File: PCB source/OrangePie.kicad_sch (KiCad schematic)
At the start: 0 parts

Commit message: Do Cleanup
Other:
- sheet 5v buck ports: added BUCK_OUT, Pgood, V_{IN}; removed 5V_OUT, Vin

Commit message: Pass ERC
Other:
- sheet DIN41612 connector ports: added 5v_STDBY, GPIOR[0..13]; removed GPIOR[0..15], STDBY OUT
- sheet FAN controller ports: added 12V_IN; removed none
- sheet OrangePi 5 pro Header ports: added BUCK_EN; removed none
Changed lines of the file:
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@@
 		(comment 2 "DESIGNED IN POLAND")
+	)
+	(junction
+		(at 67.31 138.43)
+		(diameter 0)
+		(color 0 0 0 0)
+	)
+	(junction
+		(at 135.89 142.24)
+		(diameter 0)
+		(color 0 0 0 0)
 	)
 	(no_connect
@@
 		(at 147.32 57.15)
 	)
+	(wire
+		(pts
+			(xy 135.89 142.24) (xy 147.32 142.24)
+		)
+		(stroke
+			(width 0)
+			(type default)
+		)
+	)
+	(wire
+		(pts
+			(xy 123.19 142.24) (xy 135.89 142.24)
+		)
+		(stroke
+			(width 0)
+			(type default)
+		)
+	)
 	(bus
 		(pts
@@
 		)
 	)
+	(wire
+		(pts
+			(xy 135.89 152.4) (xy 135.89 142.24)
+		)
+		(stroke
+			(width 0)
+			(type default)
+		)
+	)
 	(bus
 		(pts
@@
 	(wire
 		(pts
+			(xy 274.32 133.35) (xy 279.4 133.35)
+		)
+		(stroke
+			(width 0)
+			(type default)
+		)
+	)
+	(wire
+		(pts
 			(xy 232.41 96.52) (xy 240.03 96.52)
 		)
@@
 	(wire
 		(pts
-			(xy 232.41 53.34) (xy 240.03 53.34)
+			(xy 232.41 133.35) (xy 240.03 133.35)
 		)
 		(stroke
@@
 	(wire
 		(pts
-			(xy 50.8 120.65) (xy 104.14 120.65)
+			(xy 279.4 158.75) (xy 67.31 158.75)
 		)
 		(stroke
@@
 	(wire
 		(pts
-			(xy 50.8 138.43) (xy 147.32 138.43)
-		)
-		(stroke
-			(width 0)
-			(type default)
-		)
-	)
-	(wire
-		(pts
-			(xy 140.97 120.65) (xy 147.32 120.65)
+			(xy 190.5 135.89) (xy 185.42 135.89)
+		)
+		(stroke
+			(width 0)
+			(type default)
+		)
+	)
+	(wire
+		(pts
+			(xy 185.42 152.4) (xy 135.89 152.4)
+		)
+		(stroke
+			(width 0)
+			(type default)
+		)
+	)
+	(wire
+		(pts
+			(xy 50.8 138.43) (xy 67.31 138.43)
 		)
 		(stroke
@@
 		)
 	)
+	(wire
+		(pts
+			(xy 50.8 120.65) (xy 147.32 120.65)
+		)
+		(stroke
+			(width 0)
+			(type default)
+		)
+	)
+	(wire
+		(pts
+			(xy 185.42 135.89) (xy 185.42 152.4)
+		)
+		(stroke
+			(width 0)
+			(type default)
+		)
+	)
 	(bus
 		(pts
@@
 		)
 	)
+	(wire
+		(pts
+			(xy 67.31 138.43) (xy 86.36 138.43)
+		)
+		(stroke
+			(width 0)
+			(type default)
+		)
+	)
+	(wire
+		(pts
+			(xy 67.31 158.75) (xy 67.31 138.43)
+		)
+		(stroke
+			(width 0)
+			(type default)
+		)
+	)
 	(bus
 		(pts
@@
 	(wire
 		(pts
-			(xy 140.97 127) (xy 147.32 127)
+			(xy 123.19 135.89) (xy 147.32 135.89)
+		)
+		(stroke
+			(width 0)
+			(type default)
+		)
+	)
+	(wire
+		(pts
+			(xy 279.4 133.35) (xy 279.4 158.75)
 		)
 		(stroke
@@
 		)
 		(pin "BUCK_IN" input
+			(at 147.32 135.89 180)
+			(effects
+				(font
+					(size 1.27 1.27)
+				)
+				(justify left)
+			)
+		)
+		(pin "STDBY_IN" input
 			(at 147.32 120.65 180)
 			(effects
@@
 			)
 		)
-		(pin "STDBY_IN" input
-			(at 147.32 138.43 180)
-			(effects
-				(font
-					(size 1.27 1.27)
-				)
-				(justify left)
-			)
-		)
 		(pin "~{STDBY EN}" input
-			(at 147.32 127 180)
+			(at 147.32 142.24 180)
 			(effects
 				(font
@@
 		)
 		(pin "12V out" input
-			(at 50.8 120.65 0)
-			(effects
-				(font
-					(size 1.27 1.27)
-				)
-				(justify right)
-			)
-		)
-		(pin "STDBY OUT" input
 			(at 50.8 138.43 0)
 			(effects
@@
 			)
 		)
-		(pin "GPIOR[0..15]" input
-			(at 50.8 53.34 0)
-			(effects
-				(font
-					(size 1.27 1.27)
-				)
-				(justify right)
-			)
-		)
 		(pin "CAN2_TR_OUT{CAN}" input
 			(at 50.8 64.77 0)
@@
 		(pin "USB_DEBUG{USB}" input
 			(at 50.8 106.68 0)
+			(effects
+				(font
+					(size 1.27 1.27)
+				)
+				(justify right)
+			)
+		)
+		(pin "5v_STDBY" input
+			(at 50.8 120.65 0)
+			(effects
+				(font
+					(size 1.27 1.27)
+				)
+				(justify right)
+			)
+		)
+		(pin "GPIOR[0..13]" input
+			(at 50.8 53.34 0)
 			(effects
 				(font
@@
 		)
 		(pin "FAN_PWM" output
-			(at 232.41 53.34 0)
+			(at 232.41 133.35 0)
 			(effects
 				(font
@@
 				)
 				(justify right)
+			)
+		)
+		(pin "BUCK_EN" input
+			(at 190.5 135.89 180)
+			(effects
+				(font
+					(size 1.27 1.27)
+				)
+				(justify left)
 			)
 		)
@@
 	)
 	(sheet
-		(at 240.03 40.64)
+		(at 240.03 120.65)
 		(size 34.29 25.4)
 		(fields_autoplaced yes)
@@
 		)
 		(property "Sheetname" "FAN controller"
-			(at 240.03 39.9284 0)
+			(at 240.03 119.9384 0)
 			(effects
 				(font
@@
 		)
 		(property "Sheetfile" "FAN controller.kicad_sch"
-			(at 240.03 66.6246 0)
+			(at 240.03 146.6346 0)
 			(effects
 				(font
@@
 		)
 		(pin "FAN_PWM" input
-			(at 240.03 53.34 180)
-			(effects
-				(font
-					(size 1.27 1.27)
-				)
-				(justify left)
+			(at 240.03 133.35 180)
+			(effects
+				(font
+					(size 1.27 1.27)
+				)
+				(justify left)
+			)
+		)
+		(pin "12V_IN" input
+			(at 274.32 133.35 0)
+			(effects
+				(font
+					(size 1.27 1.27)
+				)
+				(justify right)
 			)
 		)
@@
 	)
 	(sheet
-		(at 104.14 115.57)
+		(at 86.36 130.81)
 		(size 36.83 15.24)
 		(fields_autoplaced yes)
@@
 		)
 		(property "Sheetname" "5v buck"
-			(at 104.14 114.8584 0)
+			(at 86.36 130.0984 0)
 			(effects
 				(font
@@
 		)
 		(property "Sheetfile" "5v buck.kicad_sch"
-			(at 104.14 131.3946 0)
+			(at 86.36 146.6346 0)
 			(effects
 				(font
@@
 		)
 		(pin "V_{IN}" input
-			(at 104.14 120.65 180)
+			(at 86.36 138.43 180)
 			(effects
 				(font
@@
 		)
 		(pin "Pgood" input
-			(at 140.97 127 0)
+			(at 123.19 142.24 0)
 			(effects
 				(font
@@
 		)
 		(pin "BUCK_OUT" input
-			(at 140.97 120.65 0)
-			(effects
-				(font
+			(at 123.19 135.89 0)
+			(effects
+				(font

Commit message: Prepare board for layout
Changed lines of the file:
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@@
+		)
+	)
+	(wire
+		(pts
+			(xy 274.32 133.35) (xy 279.4 133.35)
+		)
+		(stroke
+			(width 0)
+			(type default)
+		)
+	)
+	(wire
+		(pts
+			(xy 232.41 96.52) (xy 240.03 96.52)
+		)
+		(stroke
+			(width 0)
+			(type default)
+		)
+	)
+	(wire
+		(pts
+			(xy 232.41 133.35) (xy 240.03 133.35)
+		)
+		(stroke
+			(width 0)
+			(type default)
 		)
 	)
 	(bus
 		(pts
-			(xy 50.8 106.68) (xy 190.5 106.68)
-		)
-		(stroke
-			(width 0)
-			(type default)
-		)
-	)
-	(wire
-		(pts
-			(xy 274.32 133.35) (xy 279.4 133.35)
-		)
-		(stroke
-			(width 0)
-			(type default)
-		)
-	)
-	(wire
-		(pts
-			(xy 232.41 96.52) (xy 240.03 96.52)
-		)
-		(stroke
-			(width 0)
-			(type default)
-		)
-	)
-	(wire
-		(pts
-			(xy 232.41 133.35) (xy 240.03 133.35)
+			(xy 190.5 107.95) (xy 50.8 107.95)
+		)
+		(stroke
+			(width 0)
+			(type default)
+		)
+	)
+	(bus
+		(pts
+			(xy 181.61 55.88) (xy 190.5 55.88)
 		)
 		(stroke
@@
 		(pts
 			(xy 185.42 135.89) (xy 185.42 152.4)
-		)
-		(stroke
-			(width 0)
-			(type default)
-		)
-	)
-	(bus
-		(pts
-			(xy 181.61 55.88) (xy 190.5 55.88)
 		)
 		(stroke
@@
 		)
 		(pin "USB_DEBUG{USB}" input
-			(at 50.8 106.68 0)
+			(at 50.8 107.95 0)
 			(effects
 				(font
@@
 		)
 		(pin "USB_SBC{USB}" input
-			(at 190.5 55.88 180)
+			(at 190.5 107.95 180)
 			(effects
 				(font
@@
 		)
 		(pin "USB_OUT{USB}" input
-			(at 190.5 106.68 180)
-			(effects
-				(font
+			(at 190.5 55.88 180)
+			(effects
+				(font

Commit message: Prepare for boardhouse
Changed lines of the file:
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@@
+		)
+	)
+	(symbol
+		(lib_id "Graphic:SYM_ESD_Large")
+		(at 36.83 162.56 0)
+		(unit 1)
+		(exclude_from_sim no)
+		(in_bom no)
+		(on_board no)
+		(dnp no)
+		(fields_autoplaced yes)
+		(property "Reference" "#SYM1"
+			(at 36.83 157.48 0)
+			(effects
+				(font
+					(size 1.27 1.27)
+				)
+				(hide yes)
+			)
+		)
+		(property "Value" "SYM_ESD_Large"
+			(at 36.83 168.91 0)
+			(effects
+				(font
+					(size 1.27 1.27)
+				)
+				(hide yes)
+			)
+		)
+		(property "Footprint" "Symbol:ESD-Logo_6.6x6mm_SilkScreen"
+			(at 36.703 163.322 0)
+			(effects
+				(font
+					(size 1.27 1.27)
+				)
+				(hide yes)
+			)
+		)
+		(property "Datasheet" "~"
+			(at 36.703 163.322 0)
+			(effects
+				(font
+					(size 1.27 1.27)
+				)
+				(hide yes)
+			)
+		)
+		(property "Description" "ESD warning/\"Do not touch\" symbol, large"
+			(at 36.83 162.56 0)
+			(effects
+				(font
+					(size 1.27 1.27)
+				)
+				(hide yes)
+			)
+		)
+		(property "Sim.Enable" "0"
+			(at 36.83 162.56 0)
+			(effects
+				(font
+					(size 1.27 1.27)
+				)
+				(hide yes)
+			)
+		)
+		(instances
+			(project ""
+				(path "/3103c9de-f1ba-4d51-8bfc-798df1c75e2f"
+					(reference "#SYM1")
+					(unit 1)
+				)
+			)
 		)
 	)

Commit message: Fix schematic
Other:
- added sheet CAN pwr sw (CAN pwr sw.kicad_sch)
- sheet Audio Codec ports: added DAC reset; removed none
- sheet Can Transiver ports: added CAN_3V3; removed none
- sheet Can Transiver1 ports: added CAN_3V3; removed none
- sheet OrangePi 5 pro Header ports: added CAN RST, DAC RST; removed none
- sheet USB-CAN ports: added NRST; removed none

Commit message: production ready
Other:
- sheet CAN pwr sw ports: added CAN_3V3_ON; removed none
- sheet OrangePi 5 pro Header ports: added CAN_3V3_ON; removed none
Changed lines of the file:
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@@
+		)
+	)
+	(wire
+		(pts
+			(xy 54.61 111.76) (xy 54.61 80.01)
+		)
+		(stroke
+			(width 0)
+			(type default)
 		)
 	)
@@
 		(pts
 			(xy 123.19 135.89) (xy 147.32 135.89)
+		)
+		(stroke
+			(width 0)
+			(type default)
+		)
+	)
+	(wire
+		(pts
+			(xy 190.5 111.76) (xy 54.61 111.76)
+		)
+		(stroke
+			(width 0)
+			(type default)
+		)
+	)
+	(wire
+		(pts
+			(xy 54.61 80.01) (xy 69.85 80.01)
 		)
 		(stroke
@@
 	)
 	(sheet
-		(at 58.42 77.47)
-		(size 38.1 5.08)
+		(at 69.85 77.47)
+		(size 26.67 5.08)
 		(exclude_from_sim no)
 		(in_bom yes)
@@
 		)
 		(property "Sheetname" "CAN pwr sw"
-			(at 58.42 76.7584 0)
+			(at 69.85 76.7584 0)
 			(effects
 				(font
@@
 		)
 		(property "Sheetfile" "CAN pwr sw.kicad_sch"
-			(at 58.42 83.1346 0)
+			(at 69.85 83.1346 0)
 			(effects
 				(font
@@
 				)
 				(justify right)
+			)
+		)
+		(pin "CAN_3V3_ON" input
+			(at 69.85 80.01 180)
+			(effects
+				(font
+					(size 1.27 1.27)
+				)
+				(justify left)
 			)
 		)
@@
 			(effects
 				(font
+					(size 1.27 1.27)
+				)
+				(justify left)
+			)
+		)
+		(pin "CAN_3V3_ON" output
+			(at 190.5 111.76 180)
+			(effects
+				(font

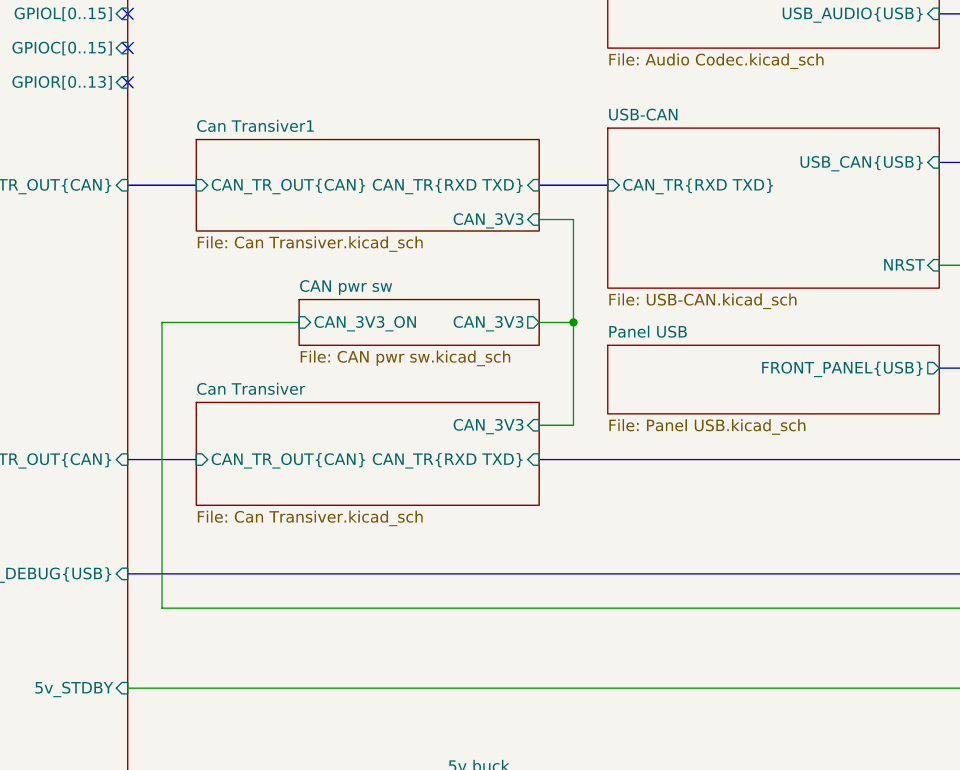
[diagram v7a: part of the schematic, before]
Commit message: Fix can power delivery , fixed placment of the mosfets, CAN power  pull down to avoid DFU boot, added new porgraming connector
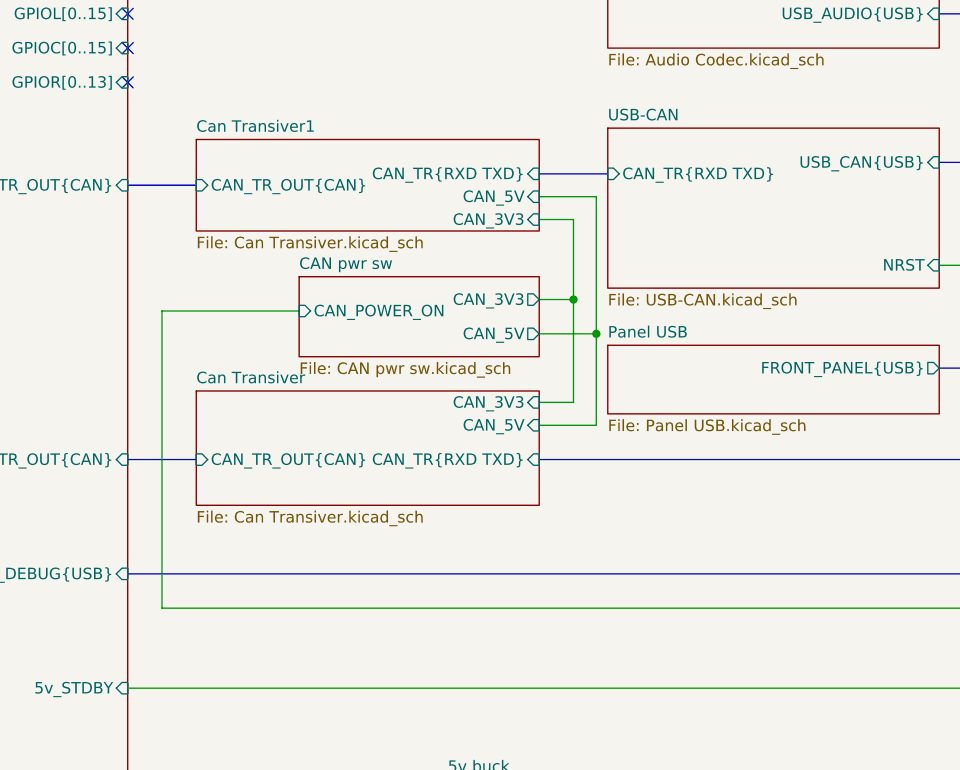
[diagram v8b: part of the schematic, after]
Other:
- sheet CAN pwr sw ports: added CAN_5V, CAN_POWER_ON; removed CAN_3V3_ON
- sheet Can Transiver ports: added CAN_5V; removed none
- sheet Can Transiver1 ports: added CAN_5V; removed none
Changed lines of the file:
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@@
+	)
+	(junction
+		(at 100.33 77.47)
+		(diameter 0)
+		(color 0 0 0 0)
 	)
 	(junction
@@
 	)
 	(junction
-		(at 100.33 80.01)
+		(at 102.87 81.28)
 		(diameter 0)
 		(color 0 0 0 0)
@@
 	(bus
 		(pts
-			(xy 96.52 64.77) (xy 104.14 64.77)
-		)
-		(stroke
-			(width 0)
-			(type default)
-		)
-	)
-	(wire
-		(pts
-			(xy 96.52 80.01) (xy 100.33 80.01)
-		)
-		(stroke
-			(width 0)
-			(type default)
-		)
-	)
-	(wire
-		(pts
-			(xy 54.61 111.76) (xy 54.61 80.01)
+			(xy 96.52 63.5) (xy 104.14 63.5)
+		)
+		(stroke
+			(width 0)
+			(type default)
+		)
+	)
+	(wire
+		(pts
+			(xy 96.52 77.47) (xy 100.33 77.47)
+		)
+		(stroke
+			(width 0)
+			(type default)
+		)
+	)
+	(wire
+		(pts
+			(xy 96.52 66.04) (xy 102.87 66.04)
+		)
+		(stroke
+			(width 0)
+			(type default)
+		)
+	)
+	(wire
+		(pts
+			(xy 54.61 111.76) (xy 54.61 78.74)
 		)
 		(stroke
@@
 	(wire
 		(pts
+			(xy 102.87 91.44) (xy 96.52 91.44)
+		)
+		(stroke
+			(width 0)
+			(type default)
+		)
+	)
+	(wire
+		(pts
 			(xy 190.5 135.89) (xy 185.42 135.89)
 		)
@@
 	(wire
 		(pts
-			(xy 100.33 80.01) (xy 100.33 91.44)
-		)
-		(stroke
-			(width 0)
-			(type default)
-		)
-	)
-	(wire
-		(pts
 			(xy 50.8 138.43) (xy 67.31 138.43)
 		)
@@
 	(wire
 		(pts
+			(xy 100.33 77.47) (xy 100.33 88.9)
+		)
+		(stroke
+			(width 0)
+			(type default)
+		)
+	)
+	(wire
+		(pts
 			(xy 185.42 135.89) (xy 185.42 152.4)
 		)
@@
 	(wire
 		(pts
-			(xy 96.52 91.44) (xy 100.33 91.44)
-		)
-		(stroke
-			(width 0)
-			(type default)
-		)
-	)
-	(wire
-		(pts
-			(xy 100.33 68.58) (xy 100.33 80.01)
+			(xy 96.52 88.9) (xy 100.33 88.9)
+		)
+		(stroke
+			(width 0)
+			(type default)
+		)
+	)
+	(wire
+		(pts
+			(xy 100.33 68.58) (xy 100.33 77.47)
 		)
 		(stroke
@@
 	(wire
 		(pts
+			(xy 96.52 81.28) (xy 102.87 81.28)
+		)
+		(stroke
+			(width 0)
+			(type default)
+		)
+	)
+	(wire
+		(pts
 			(xy 190.5 111.76) (xy 54.61 111.76)
 		)
@@
 	(wire
 		(pts
-			(xy 54.61 80.01) (xy 69.85 80.01)
+			(xy 54.61 78.74) (xy 69.85 78.74)
 		)
 		(stroke
@@
 		(pts
 			(xy 232.41 83.82) (xy 240.03 83.82)
+		)
+		(stroke
+			(width 0)
+			(type default)
+		)
+	)
+	(wire
+		(pts
+			(xy 102.87 81.28) (xy 102.87 91.44)
+		)
+		(stroke
+			(width 0)
+			(type default)
+		)
+	)
+	(wire
+		(pts
+			(xy 102.87 66.04) (xy 102.87 81.28)
 		)
 		(stroke
@@
 	)
 	(sheet
-		(at 69.85 77.47)
-		(size 26.67 5.08)
+		(at 69.85 74.93)
+		(size 26.67 8.89)
 		(exclude_from_sim no)
 		(in_bom yes)
@@
 		)
 		(property "Sheetname" "CAN pwr sw"
-			(at 69.85 76.7584 0)
+			(at 69.85 74.2184 0)
 			(effects
 				(font
@@
 		)
 		(property "Sheetfile" "CAN pwr sw.kicad_sch"
-			(at 69.85 83.1346 0)
+			(at 69.85 84.4046 0)
 			(effects
 				(font
@@
 		)
 		(pin "CAN_3V3" output
-			(at 96.52 80.01 0)
-			(effects
-				(font
-					(size 1.27 1.27)
-				)
-				(justify right)
-			)
-		)
-		(pin "CAN_3V3_ON" input
-			(at 69.85 80.01 180)
+			(at 96.52 77.47 0)
+			(effects
+				(font
+					(size 1.27 1.27)
+				)
+				(justify right)
+			)
+		)
+		(pin "CAN_5V" output
+			(at 96.52 81.28 0)
+			(effects
+				(font
+					(size 1.27 1.27)
+				)
+				(justify right)
+			)
+		)
+		(pin "CAN_POWER_ON" input
+			(at 69.85 78.74 180)
 			(effects
 				(font
@@
 		)
 		(pin "CAN_TR{RXD TXD}" input
-			(at 104.14 64.77 180)
+			(at 104.14 63.5 180)
 			(effects
 				(font
@@
 	)
 	(sheet
-		(at 58.42 88.9)
-		(size 38.1 11.43)
+		(at 58.42 87.63)
+		(size 38.1 12.7)
 		(exclude_from_sim no)
 		(in_bom yes)
@@
 		)
 		(property "Sheetname" "Can Transiver"
-			(at 58.42 88.1884 0)
+			(at 58.42 86.9184 0)
 			(effects
 				(font
@@
 		)
 		(pin "CAN_3V3" input
+			(at 96.52 88.9 0)
+			(effects
+				(font
+					(size 1.27 1.27)
+				)
+				(justify right)
+			)
+		)
+		(pin "CAN_5V" input
 			(at 96.52 91.44 0)
 			(effects
@@
 		)
 		(pin "CAN_TR{RXD TXD}" input
-			(at 96.52 64.77 0)
+			(at 96.52 63.5 0)
 			(effects
 				(font
@@
 			(effects
 				(font
+					(size 1.27 1.27)
+				)
+				(justify right)
+			)
+		)
+		(pin "CAN_5V" input
+			(at 96.52 66.04 0)
+			(effects
+				(font
